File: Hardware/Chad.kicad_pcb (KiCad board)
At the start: 4 copper layers, 30 x 60 mm, 127 parts, among them J1 RBUS, J2 GPIO Breakout, J3 ServoCH1, J4 ServoCH2, J5 USB_C_Receptacle_USB2.0, U1 ESP32-S3, U2 SN65HVD230, U3 LM66200DRLR, U4 MAX77827AEFD+T, U5 SC4215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

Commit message: updated to use 12A inductor
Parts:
- C48: moved to B.Cu
- L4: footprint iclr:SRP5050FA5R6M -> ICLR:EXL1V07053R3R
- moved C33 12.0 mm to (54.8, 90.4), turned to 180 degrees
- moved C47 11.3 mm to (59.2, 94.3), turned to 0 degrees
- moved C35 7.98 mm to (53.3, 99.7), turned to -50 degrees
- moved C49 7.70 mm to (59.2, 92.4), turned to 0 degrees
- moved C46 7.11 mm to (59.2, 90.4), turned to 0 degrees
- moved C48 6.64 mm to (53.8, 92.9), turned to 130 degrees
- moved C31 5.37 mm to (52.2, 94.6), turned to 130 degrees
- moved C37 2.53 mm to (53.7, 93.3), turned to 130 degrees
- moved L4 1.31 mm to (46.3, 96.1)
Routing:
- net GND: vias 116 -> 115
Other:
- board text added: "Board Number -"
- board text removed: "JLCJLCJLCJLC"
- board text removed: "Serial Number -"

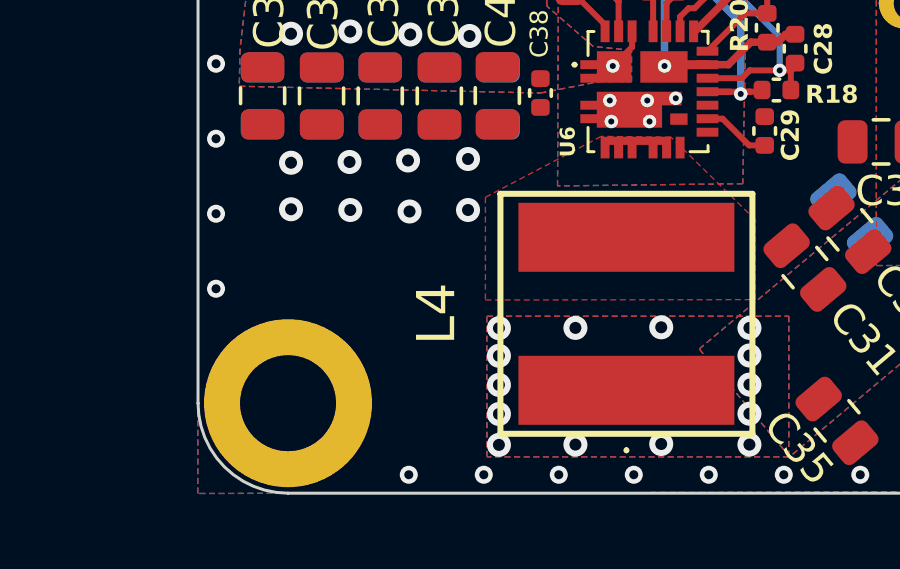
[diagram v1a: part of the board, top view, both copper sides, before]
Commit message: updated current limit resistor (oops)
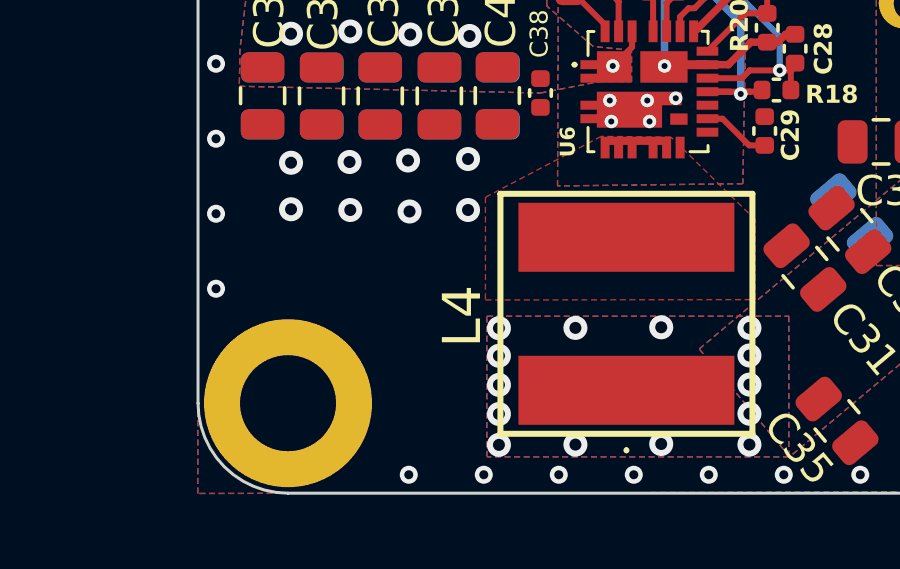
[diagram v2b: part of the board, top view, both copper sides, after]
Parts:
- L4: value 5.6uH -> 3.3uH; footprint ICLR:EXL1V07053R3R -> iclr:EXL1V07053R3R
- R22: value 100k -> 200k

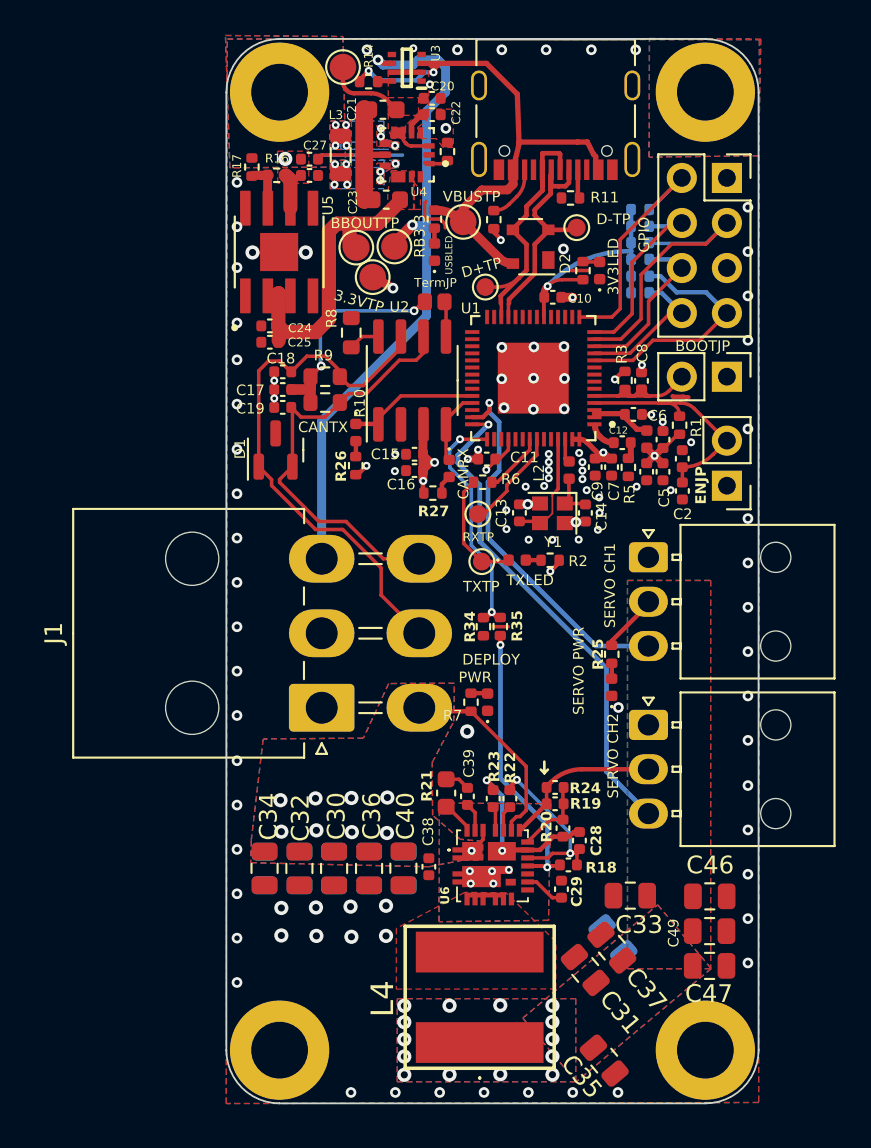
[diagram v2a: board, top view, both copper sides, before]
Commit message: jlc order number location specified, slightly better can routing
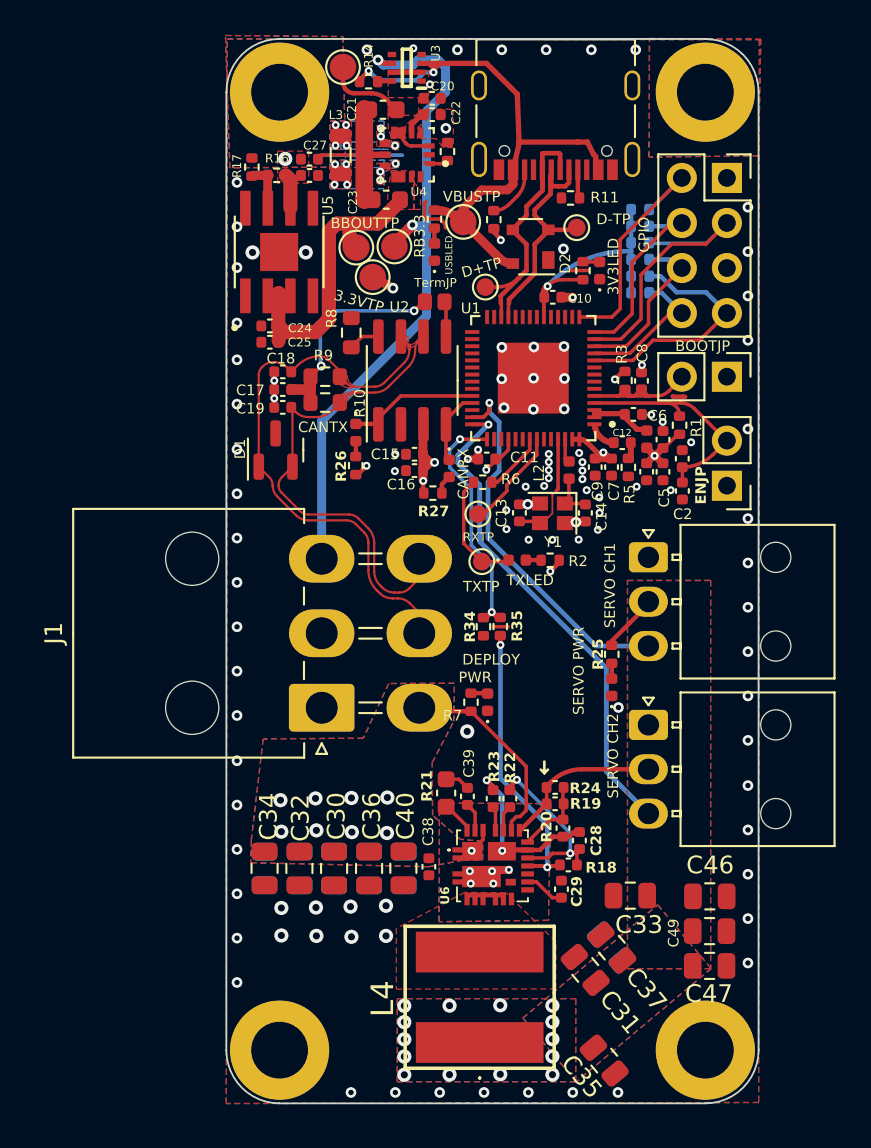
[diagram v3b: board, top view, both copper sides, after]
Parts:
- moved C48 0.41 mm to (53.7, 93.3)
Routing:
- net /CAN-: track 24.3 -> 27.7 mm
- net /CAN+: track 30.7 -> 33.1 mm
- added copper zone on F.Cu, net /CAN+
- added copper zone on F.Cu, net /CAN-
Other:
- board text added: "Batch Number - JLCJLCJLCJLC"
